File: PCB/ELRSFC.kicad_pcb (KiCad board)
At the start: 2 copper layers, 33 x 33 mm, 98 parts, among them J1 Conn_Coaxial_Small, Q1 2N7002, U1 W25Q128JVSIQTR, U2 XL1509-5.0E1, U4 AT7456E, U5 MPU6500, U6 STM32F411CEU6, U7 ESP8285H16, U8 SX1281IMLTRT, U9 SPX3819M5-L-3-3/TR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

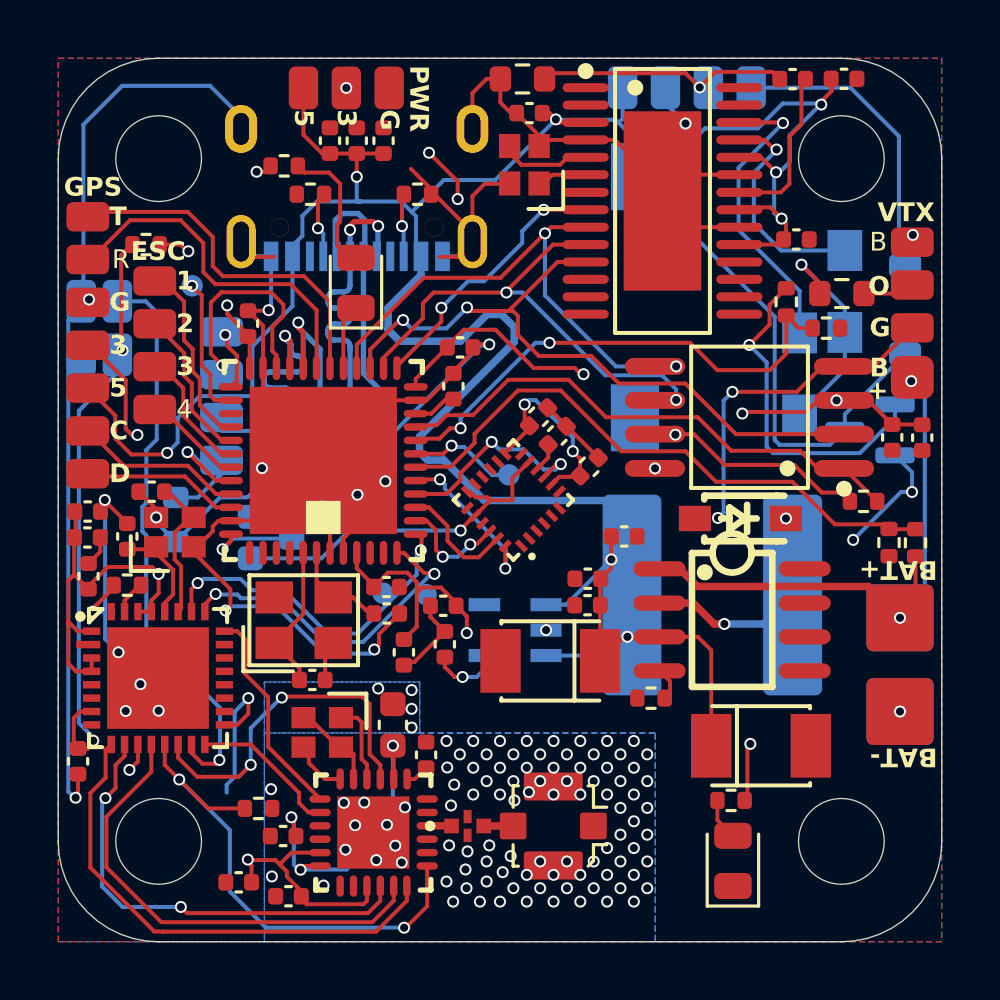
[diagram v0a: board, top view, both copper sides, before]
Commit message: Added 0.15mm board size on each edge for v cut clearance
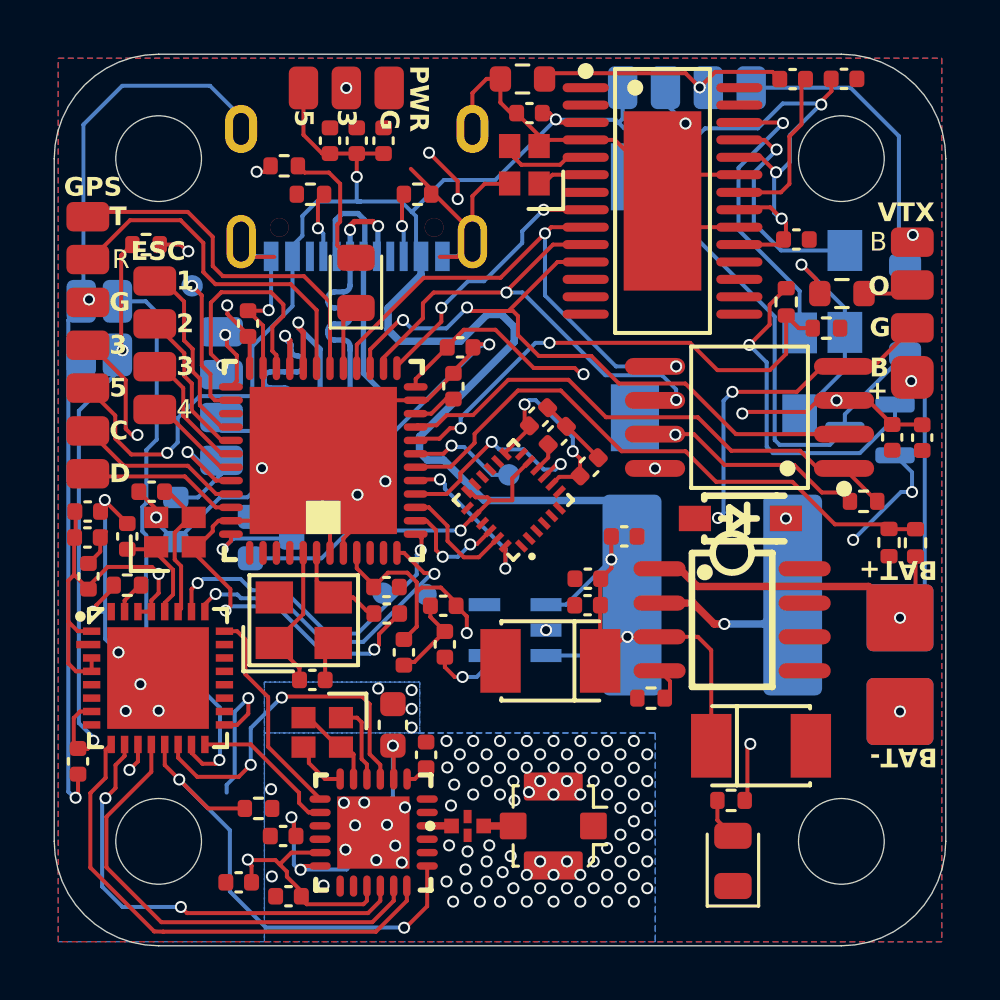
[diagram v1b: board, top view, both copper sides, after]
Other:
- board size 33 x 33 mm -> 33.3 x 33.3 mm
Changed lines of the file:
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@@
 	)
 	(gr_arc
-		(start 177 61.75)
-		(mid 179.65165 62.84835)
-		(end 180.75 65.5)
+		(start 147.6 65.5)
+		(mid 148.742284 62.742284)
+		(end 151.5 61.6)
 		(stroke
 			(width 0.05)
@@
 	)
 	(gr_line
-		(start 180.75 65.5)
-		(end 180.75 91)
+		(start 180.9 65.5)
+		(end 180.9 91)
 		(stroke
 			(width 0.05)
@@
 	)
 	(gr_line
-		(start 151.5 61.75)
-		(end 177 61.75)
+		(start 151.5 61.6)
+		(end 177 61.6)
+		(stroke
+			(width 0.05)
+			(type default)
+		)
+		(layer "Edge.Cuts")
+	)
+	(gr_line
+		(start 177 94.9)
+		(end 151.5 94.9)
+		(stroke
+			(width 0.05)
+			(type default)
+		)
+		(layer "Edge.Cuts")
+	)
+	(gr_line
+		(start 147.6 91)
+		(end 147.6 65.5)
 		(stroke
 			(width 0.05)
@@
 	)
 	(gr_arc
-		(start 180.75 91)
-		(mid 179.65165 93.65165)
-		(end 177 94.75)
-		(stroke
-			(width 0.05)
-			(type default)
-		)
-		(layer "Edge.Cuts")
-	)
-	(gr_line
-		(start 177 94.75)
-		(end 151.5 94.75)
-		(stroke
-			(width 0.05)
-			(type default)
-		)
-		(layer "Edge.Cuts")
-	)
-	(gr_line
-		(start 147.75 91)
-		(end 147.75 65.5)
+		(start 177 61.6)
+		(mid 179.757716 62.742284)
+		(end 180.9 65.5)
 		(stroke
 			(width 0.05)
@@
 	)
 	(gr_arc
-		(start 151.5 94.75)
-		(mid 148.84835 93.65165)
-		(end 147.75 91)
+		(start 180.9 91)
+		(mid 179.757716 93.757716)
+		(end 177 94.9)
 		(stroke
 			(width 0.05)
@@
 	)
 	(gr_arc
-		(start 147.75 65.5)
-		(mid 148.84835 62.84835)
-		(end 151.5 61.75)
+		(start 151.5 94.9)
+		(mid 148.742284 93.757716)
+		(end 147.6 91)
 		(stroke
 			(width 0.05)
